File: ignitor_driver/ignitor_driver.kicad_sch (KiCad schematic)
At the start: 53 parts, among them J1 Conn_02x05_Counter_Clockwise, J2 24V_IN, J3 GND_IN, J4 Conn_02x01, K1 G5LE-1 DC24, K2 G5LE-1 DC24, K3 G5LE-1 DC24, Q1 PMOS, Q2 BSS138, Q3 BSS138, Q4 BSS138, U1 LM4040DBZ-2.5, U2 LM4040DBZ-2.5, U3 TLV333IDBVR, U4 OPA990IDBVR, U5 AMC3330, U6 ACS724xLCTR-30AU

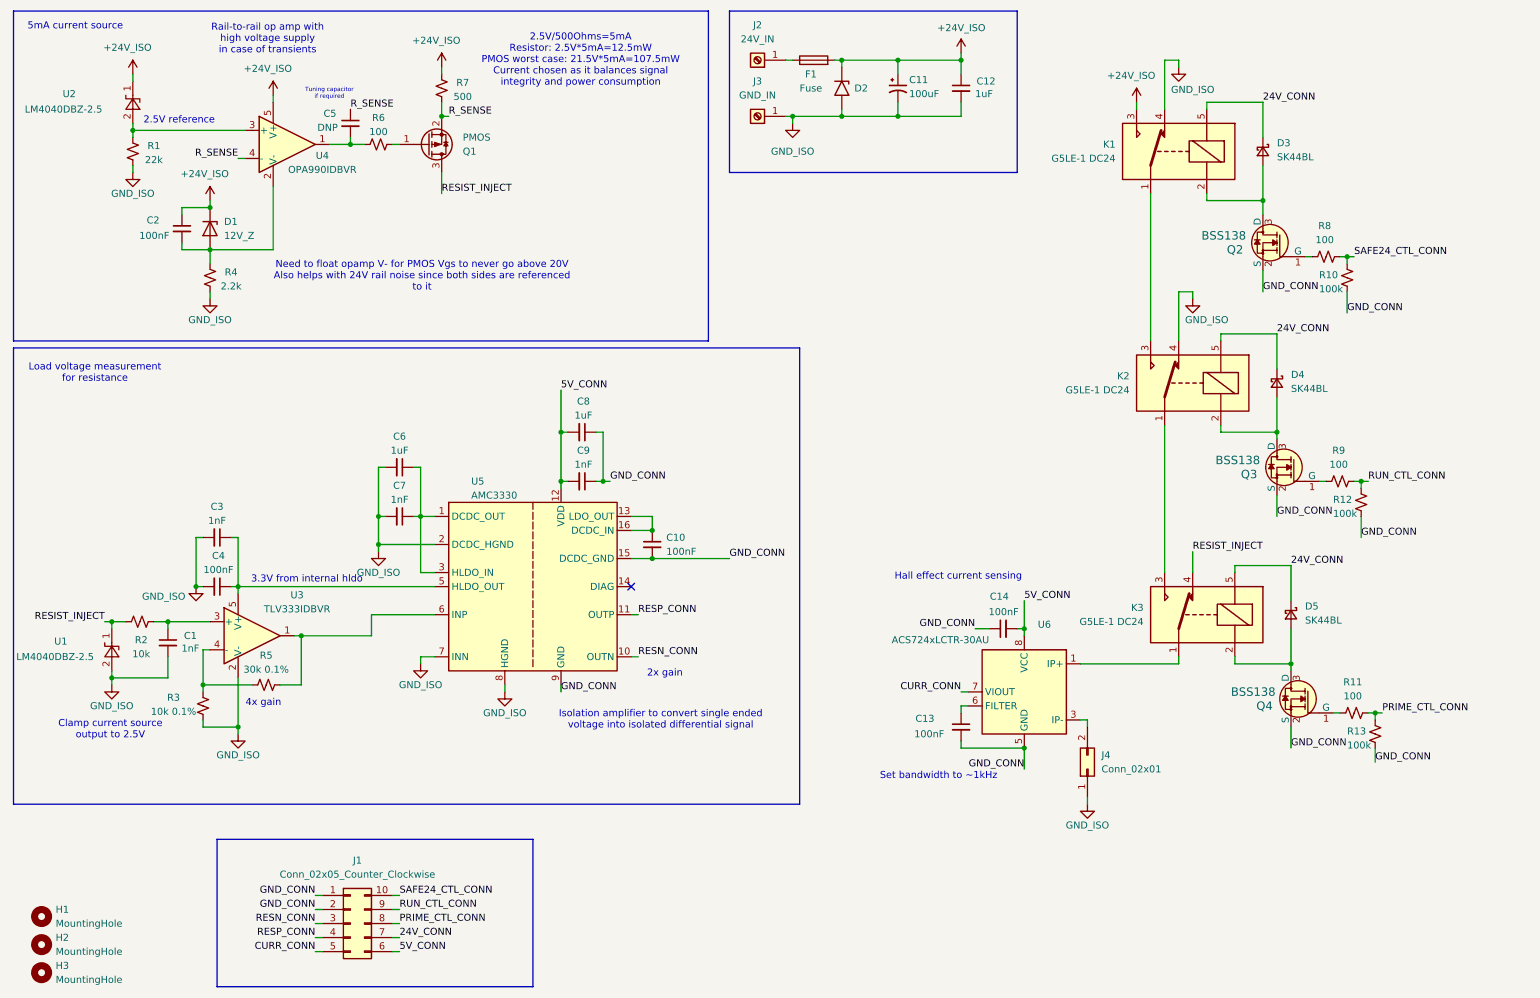
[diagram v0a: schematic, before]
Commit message: improve silkscreening on ignitor board and add connector for keyswitch
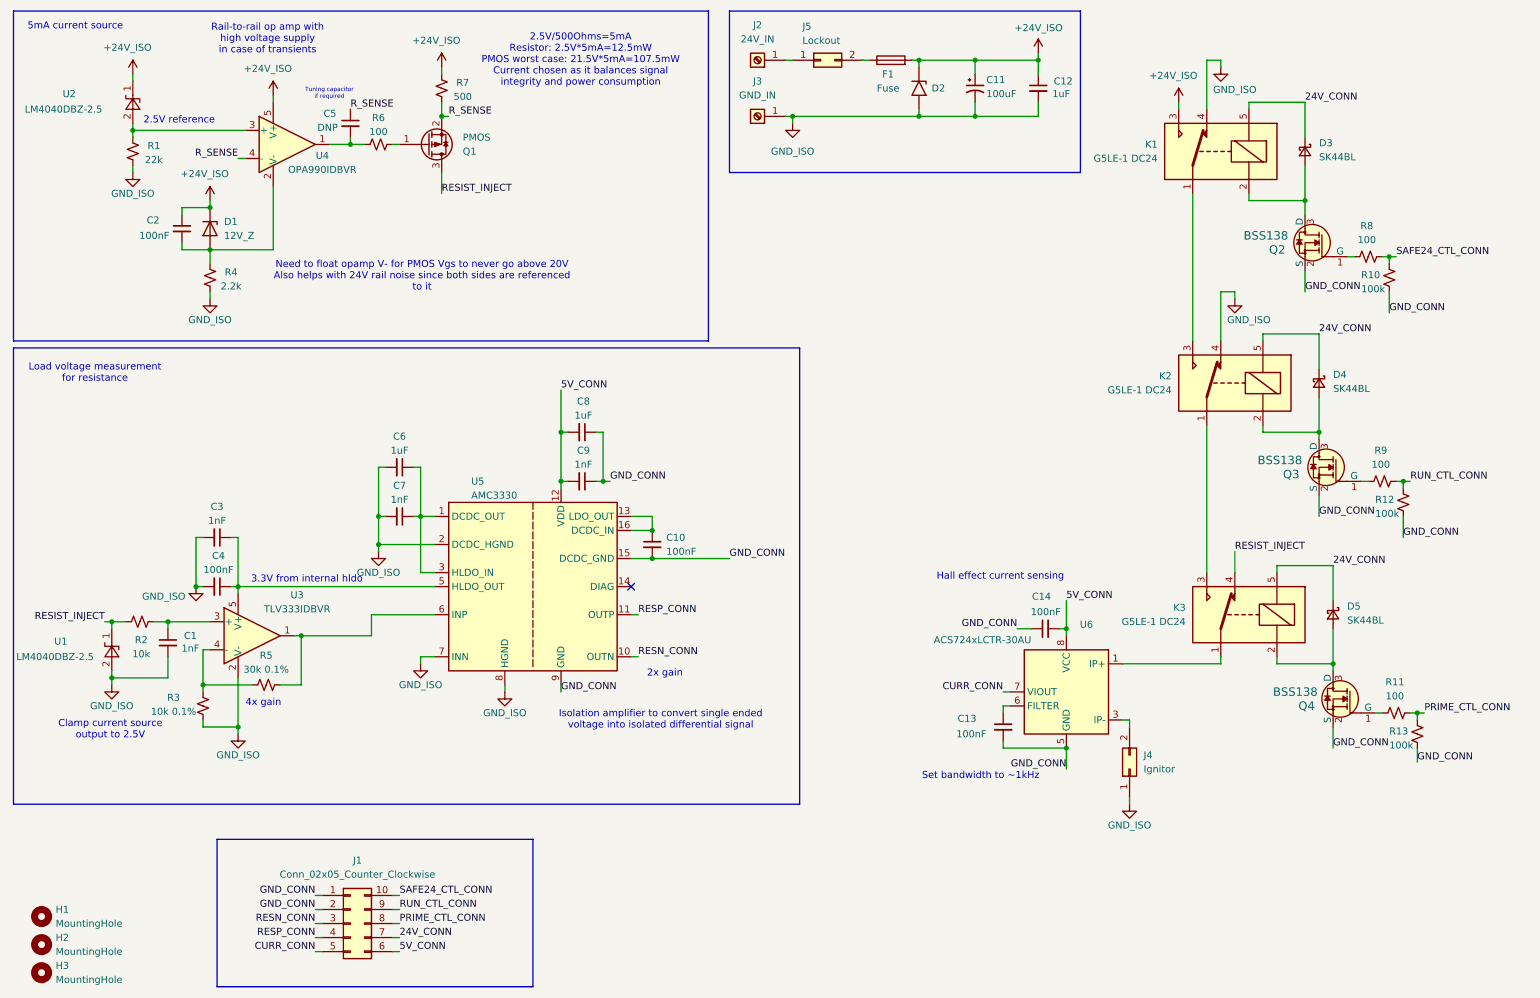
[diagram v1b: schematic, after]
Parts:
- added J5: Lockout, Connector_Molex:Molex_Mini-Fit_Jr_5566-02A_2x01_P4.20mm_Vertical, symbol Connector_Generic:Conn_02x01
- J4: value Conn_02x01 -> Ignitor
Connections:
- net at J2.1 (Pin_1): now also J5.1 (Pin_1); no longer F1.1
- new net: F1.1, J5.2 (Pin_2)
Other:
- moved on the sheet: C11, C12, C13, C14, D2, D3, D4, D5, F1, J4, K1, K2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
